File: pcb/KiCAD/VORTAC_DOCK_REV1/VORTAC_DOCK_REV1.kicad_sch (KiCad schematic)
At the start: 27 parts, among them J1 Conn_01x05, J2 Conn_01x03, J3 Screw_Terminal_01x02, J4 Conn_01x03, J5 Conn_01x04, J6 Conn_01x04, U1 WS2811, U2 TPS26630RGE, U6 AP63205WU

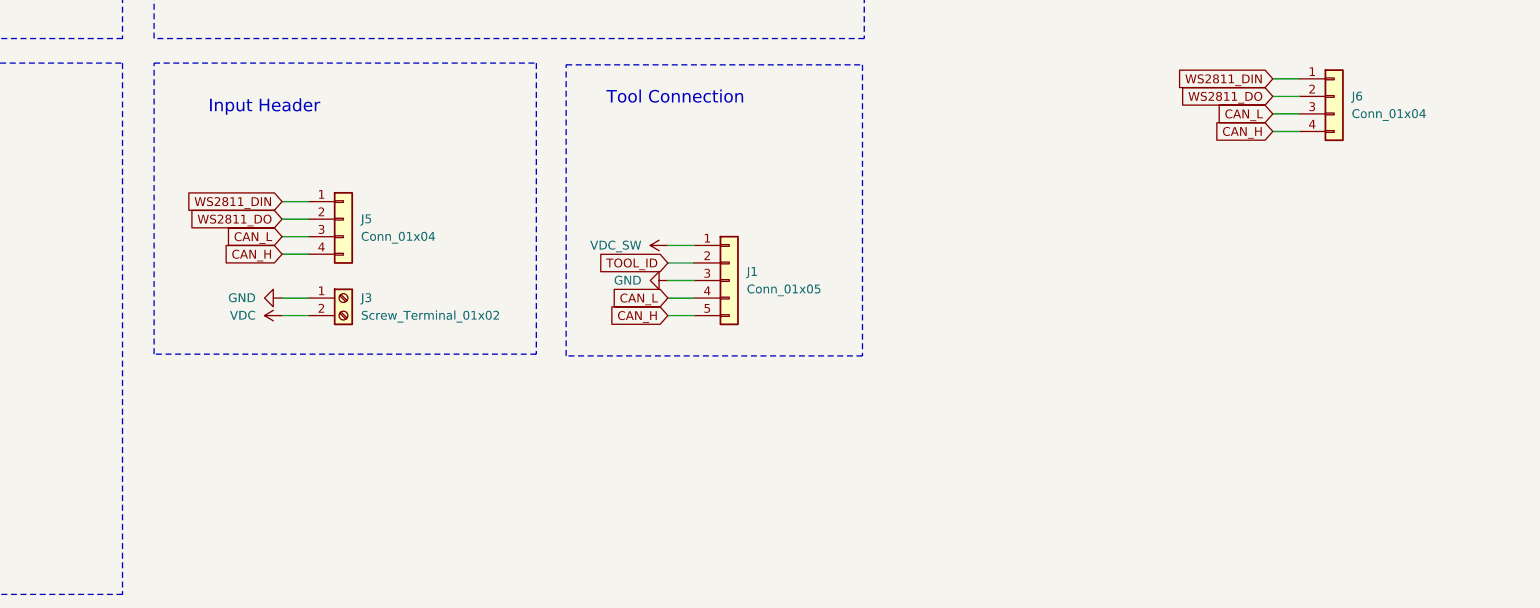
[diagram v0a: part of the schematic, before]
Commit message: new Footprints and replaced chonky connectors
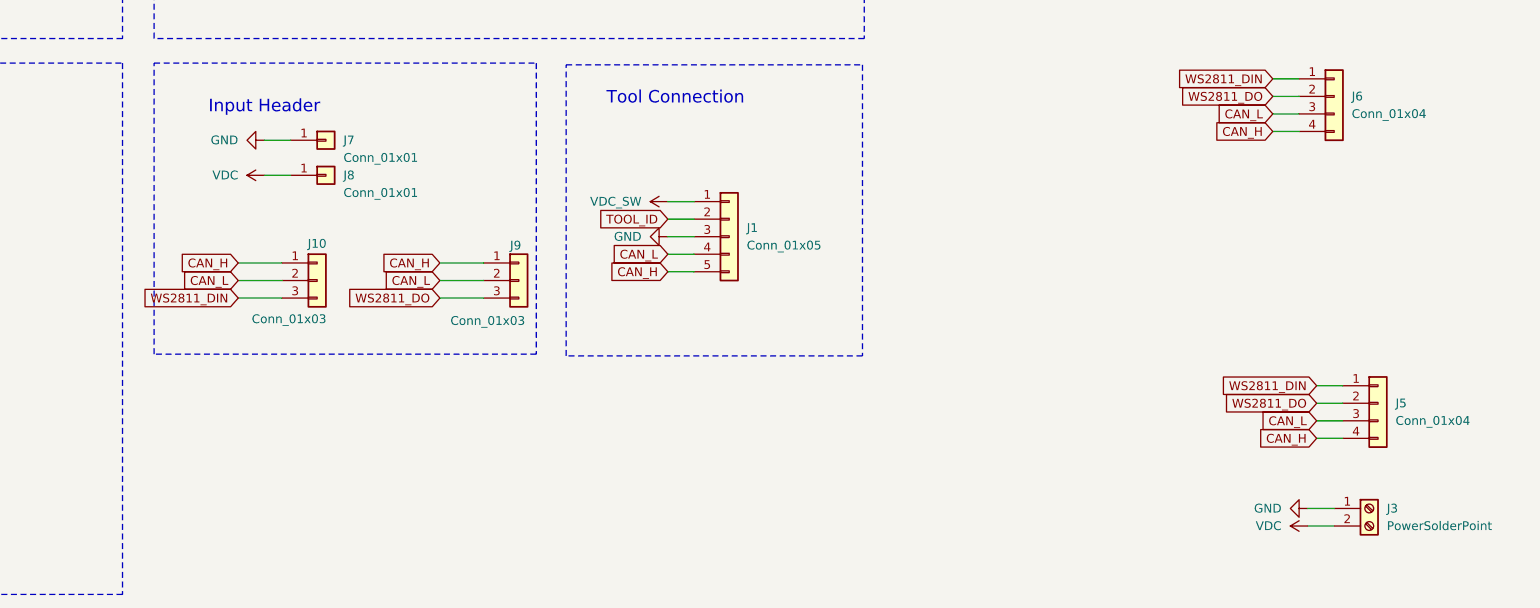
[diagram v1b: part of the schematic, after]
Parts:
- added J10, J9: Conn_01x03, Vortac:Solderpoint_01x03_Data, symbol Connector_Generic:Conn_01x03
- added J7: Conn_01x01, Vortac:Dock_Solderpoint_02x01_GND, symbol Connector_Generic:Conn_01x01
- added J8: Conn_01x01, Vortac:Dock_Solderpoint_02x01_VCC, symbol Connector_Generic:Conn_01x01
- J3: value Screw_Terminal_01x02 -> PowerSolderPoint; footprint TerminalBlock:TerminalBlock_MaiXu_MX126-5.0-02P_1x02_P5.00mm -> Vortac:Dock_Solderpoint_02x02_Power
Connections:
- net CAN_H: now also J10.1 (Pin_1), J9.1 (Pin_1)
- net CAN_L: now also J10.2 (Pin_2), J9.2 (Pin_2)
- net GND: now also J7.1 (Pin_1)
- net VDC: now also J8.1 (Pin_1)
- net WS2811_DIN: now also J10.3 (Pin_3)
- net WS2811_DO: now also J9.3 (Pin_3)
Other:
- moved on the sheet: J1, J3, J5

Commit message: Vortac Dock rough component placement #NO-JIRA
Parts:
- added JP1: SolderJumper_2_Open, Vortac:SolderJumper_Hex_Open_Pad, symbol Jumper:SolderJumper_2_Open
- added JP2: SolderJumper_2_Open, Jumper:SolderJumper-2_P1.3mm_Open_RoundedPad1.0x1.5mm, symbol Jumper:SolderJumper_2_Open
- added R16: 120R, Resistor_SMD:R_0402_1005Metric, symbol Device:R_Small
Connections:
- net CAN_H: now also R16.2
- net CAN_L: now also JP1.2 (B)
- new net: JP1.1 (A), R16.1
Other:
- note added: "Can Termination"
- moved on the sheet: D1, D6, D7, H1, H2, J1, J10, J3, J5, J7, J8, J9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

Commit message: Check Lcsc numbers
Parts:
- C30, C31: notes could be 10V maybe 0402 -> (none)
- D1, J1, J10, J2, J3, J4, J5, J6, J7, J8, J9: now left out of the parts list
- D7: LCSC C130724 -> C130719
- R13: LCSC C60490 -> C137987
- R15: value 170K -> 165K; LCSC C60490 -> C42396631
- R16: LCSC (none) -> C114758
- R38: LCSC (none) -> C106232
- R39: LCSC (none) -> C477610
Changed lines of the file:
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@@
 			)
 		)
-		(property "LCSC" ""
+		(property "LCSC" "C106232"
 			(at 189.23 38.1 90)
 			(effects
@@
 		(unit 1)
 		(exclude_from_sim no)
-		(in_bom yes)
+		(in_bom no)
 		(on_board no)
 		(dnp no)
@@
 		(unit 1)
 		(exclude_from_sim no)
-		(in_bom yes)
+		(in_bom no)
 		(on_board no)
 		(dnp no)
@@
 		(unit 1)
 		(exclude_from_sim no)
-		(in_bom yes)
+		(in_bom no)
 		(on_board no)
 		(dnp no)
@@
 		(unit 1)
 		(exclude_from_sim no)
-		(in_bom yes)
+		(in_bom no)
 		(on_board yes)
 		(dnp no)
@@
 			)
 		)
-		(property "LCSC" "C60490"
+		(property "LCSC" "C137987"
 			(at 100.33 168.91 0)
 			(effects
@@
 		(unit 1)
 		(exclude_from_sim no)
-		(in_bom yes)
+		(in_bom no)
 		(on_board no)
 		(dnp no)
@@
 			)
 		)
-		(property "LCSC" ""
+		(property "LCSC" "C477610"
 			(at 189.23 45.72 90)
 			(effects
@@
 		(unit 1)
 		(exclude_from_sim no)
-		(in_bom yes)
+		(in_bom no)
 		(on_board yes)
 		(dnp no)
@@
 		(unit 1)
 		(exclude_from_sim no)
-		(in_bom yes)
+		(in_bom no)
 		(on_board no)
 		(dnp no)
@@
 			)
 		)
-		(property "Value" "170K"
+		(property "Value" "165K"
 			(at 112.268 148.59 0)
 			(effects
@@
 			)
 		)
-		(property "LCSC" "C60490"
+		(property "LCSC" "C42396631"
 			(at 110.49 147.32 0)
 			(effects
@@
 		(unit 1)
 		(exclude_from_sim no)
-		(in_bom yes)
+		(in_bom no)
 		(on_board yes)
 		(dnp no)
@@
 			)
 		)
-		(property "Datasheet" "https://www.lcsc.com/datasheet/lcsc_datasheet_2008201033_Foshan-NationStar-Optoelectronics-NCD0402B1_C130724.pdf"
+		(property "Datasheet" "https://www.lcsc.com/datasheet/C130719.pdf"
 			(at 196.85 45.72 90)
 			(effects
@@
 			)
 		)
-		(property "LCSC" "C130724"
+		(property "LCSC" "C130719"
 			(at 196.85 45.72 0)
 			(effects
@@
 		(unit 1)
 		(exclude_from_sim no)
-		(in_bom yes)
+		(in_bom no)
 		(on_board yes)
 		(dnp no)
@@
 		(unit 1)
 		(exclude_from_sim no)
-		(in_bom yes)
+		(in_bom no)
 		(on_board yes)
 		(dnp no)
@@
 			)
 		)
-		(property "notes" "could be 10V maybe 0402"
+		(property "notes" ""
 			(at 116.84 43.18 0)
 			(effects
@@
 		(unit 1)
 		(exclude_from_sim no)
-		(in_bom yes)
+		(in_bom no)
 		(on_board no)
 		(dnp no)
@@
 			)
 		)
-		(property "notes" "could be 10V maybe 0402"
+		(property "notes" ""
 			(at 130.81 43.18 0)
 			(effects
@@
 			)
 		)
-		(property "LCSC" ""
+		(property "LCSC" "C114758"
 			(at 248.92 95.25 0)
 			(effects

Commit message: Routed Vortac Dock PCB REV1
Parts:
- removed D1: NeoPixel_THT, LED_SMD:LED_WS2812B-2020_PLCC4_2.0x2.0mm, symbol LED:NeoPixel_THT
- removed J2, J4: Conn_01x03, Connector_JST:JST_PH_B3B-PH-K_1x03_P2.00mm_Vertical, symbol Connector_Generic:Conn_01x03
- removed J3: PowerSolderPoint, Vortac:Dock_Solderpoint_02x02_Power, symbol Connector:Screw_Terminal_01x02
- removed J5: Conn_01x04, Connector_JST:JST_PH_B4B-PH-K_1x04_P2.00mm_Vertical, symbol Connector_Generic:Conn_01x04
- removed J6: Conn_01x04, Connector_JST:JST_PH_S4B-PH-K_1x04_P2.00mm_Horizontal, symbol Connector_Generic:Conn_01x04
- removed JP2: SolderJumper_2_Open, Jumper:SolderJumper-2_P1.3mm_Open_RoundedPad1.0x1.5mm, symbol Jumper:SolderJumper_2_Open
- JP1: footprint Vortac:SolderJumper_Hex_Open_Pad -> Jumper:SolderJumper-2_P1.3mm_Open_RoundedPad1.0x1.5mm
- U3: renamed from U2; footprint Package_DFN_QFN:Texas_RGE0024H_VQFN-24-1EP_4x4mm_P0.5mm_EP2.7x2.7mm_ThermalVias -> Vortac:Texas_RGE0024H_VQFN-24-1EP_4x4mm_P0.5mm_EP2.7x2.7mm_ThermalVias
- renumbered C28 to C1, C30 to C2, C31 to C3, C27 to C4, C34 to C5, C33 to C6, D6 to D1, D7 to D2, J7 to J1, J8 to J2, J1 to J3, J10 to J4, J9 to J5, L3 to L1, R38 to R1, R39 to R2, R16 to R3, R15 to R4, R14 to R5, R13 to R6, R12 to R7, U6 to U1, U1 to U2
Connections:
- net CAN_H: now also J4.2 (Pin_2), J5.2 (Pin_2); no longer J4.1 (Pin_1), J5.1 (Pin_1)
- net CAN_L: now also J4.1 (Pin_1), J5.1 (Pin_1); no longer J4.2 (Pin_2), J5.2 (Pin_2)
- net TOOL_ID: now also J3.1 (Pin_1); no longer J3.2 (Pin_2)
- net VDC_SW: now also J3.2 (Pin_2); no longer J3.1 (Pin_1)
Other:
- note removed: "ADD TERMINATION RESISTOR"

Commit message: Production Files
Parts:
- L1: LCSC C5832360 -> C2762594
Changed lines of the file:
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@@
 			)
 		)
-		(property "LCSC" "C5832360"
+		(property "LCSC" "C2762594"
 			(at 105.41 38.1 90)
 			(effects

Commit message: Doc Rev1 revision
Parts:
- added C34: 100uF 35V, Capacitor_SMD:CP_Elec_6.3x7.7, symbol Vortac:CP-Device
- added D5: PTVS26VS1UR,115-ES, Diode_SMD:D_SOD-123F, symbol Diode:SD24_SOD323
- L1: LCSC C2762594 -> C5832360
- R4: LCSC C42396631 -> C38706
- U2: footprint Package_TO_SOT_SMD:SOT-23-8 -> Vortac:SOT-23-8; 8mm pitch
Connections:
- net GND: now also C34.2, D5.2 (A2)
- net VDC: now also C34.1, D5.1 (A1)
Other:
- moved on the sheet: C4
